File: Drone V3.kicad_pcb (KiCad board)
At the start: 4 copper layers, 96 parts, among them J2 Phase Outputs, J3 Pad Terminals, J4 Signal, U1 IRS21867S, U13 STM32F303CBTx, U4 INA180A3, U6 IRS21867S, U7 IRS21867S, U8 INA180A3, U9 INA180A3

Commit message: Drone PCB Update
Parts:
- removed 12V_SD2: XL1509-12, Package_SO:SOIC-8_3.9x4.9mm_P1.27mm
- removed 3.3V_SD1: AP63203WU, Package_TO_SOT_SMD:TSOT-23-6
- removed 5V_SD1: XL1509-5, easyeda2kicad:SOIC-8_L5.0-W4.0-P1.27-LS6.0-BL
- removed D1, D6: SS34, easyeda2kicad:SMA_L4.3-W2.6-LS5.2-RD
- 12V_SD1: renamed from 12V; moved to B.Cu
- B: renamed from BOOT0_SW1; moved to B.Cu
- C15, C16, C17, C18, C19, C20, C21, C22, C23, C24, C25, C26, C27, C28, C39, C41, C42, C43, C45, C49, C50, C51, D10, D12, D8, L6, R10, R11, R12, R13, R14, R15, R16, R17, R18, R19, R20, R21, R22, R23, R24, R25, R26, R27, R28, R29, R30, R31, R34, R36, R37, R38, R39, R40, R9, ST-Link1, U1, U4, U6, U7, U8, U9: moved to B.Cu
- D14: value LED -> DBG1
- D15: value LED -> DBG2
- D17: value BuckLED -> BUCK
- R: renamed from NRST_SW1; moved to B.Cu
- U13: value STM32F303CBTx -> STM32
- moved NMOS2 154.6 mm to (48.3, 145.2), turned to 90 degrees
- moved NMOS3 149.7 mm to (36.9, 137.5), turned to 90 degrees
- moved NMOS4 125.6 mm to (48.3, 137.5), turned to 90 degrees
- moved NMOS1 124.2 mm to (36.9, 145.2), turned to 90 degrees
- moved C16 111.4 mm to (39.0, 145.5)
- moved NMOS5 111.4 mm to (36.9, 129.6), turned to 90 degrees
- moved R9 111.1 mm to (43.5, 145.5)
- moved C24 108.5 mm to (31.4, 140.5)
- moved R30 107.1 mm to (69.5, 150.5), turned to 90 degrees
- moved R10 105.7 mm to (43.5, 143.0)
- moved C18 104.6 mm to (52.5, 142.5), turned to 180 degrees
- moved C19 104.1 mm to (52.5, 145.0), turned to 180 degrees
- moved R31 103.6 mm to (67.0, 150.5), turned to -90 degrees
- moved B 102.6 mm to (73.5, 150.5), turned to 180 degrees
- moved R36 101.6 mm to (56.5, 145.0)
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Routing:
- net /ESC1/-ESC: track 14.6 -> 0.00 mm
- net /ESC1/+ESC: track 11.8 -> 0.00 mm
- net Net-(D15-A): track 2.62 -> 0.00 mm
- net Net-(D14-A): track 2.62 -> 0.00 mm
- net Net-(D17-K): track 2.56 -> 0.00 mm
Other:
- board outline added: 55 x 30 mm
- board text added: "12V"
- board text added: "DB1"
- board text added: "DB2"

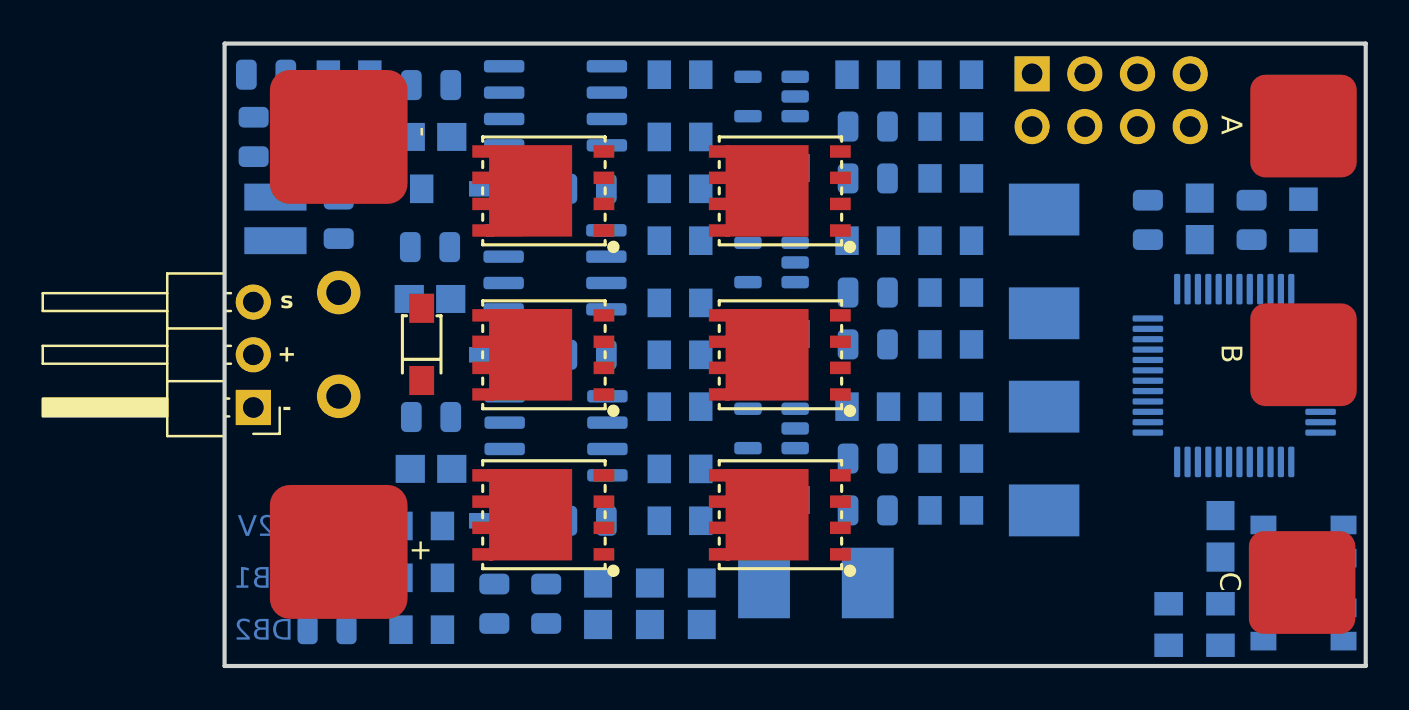
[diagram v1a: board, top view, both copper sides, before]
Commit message: ESC Routing, MOS Footprint Change
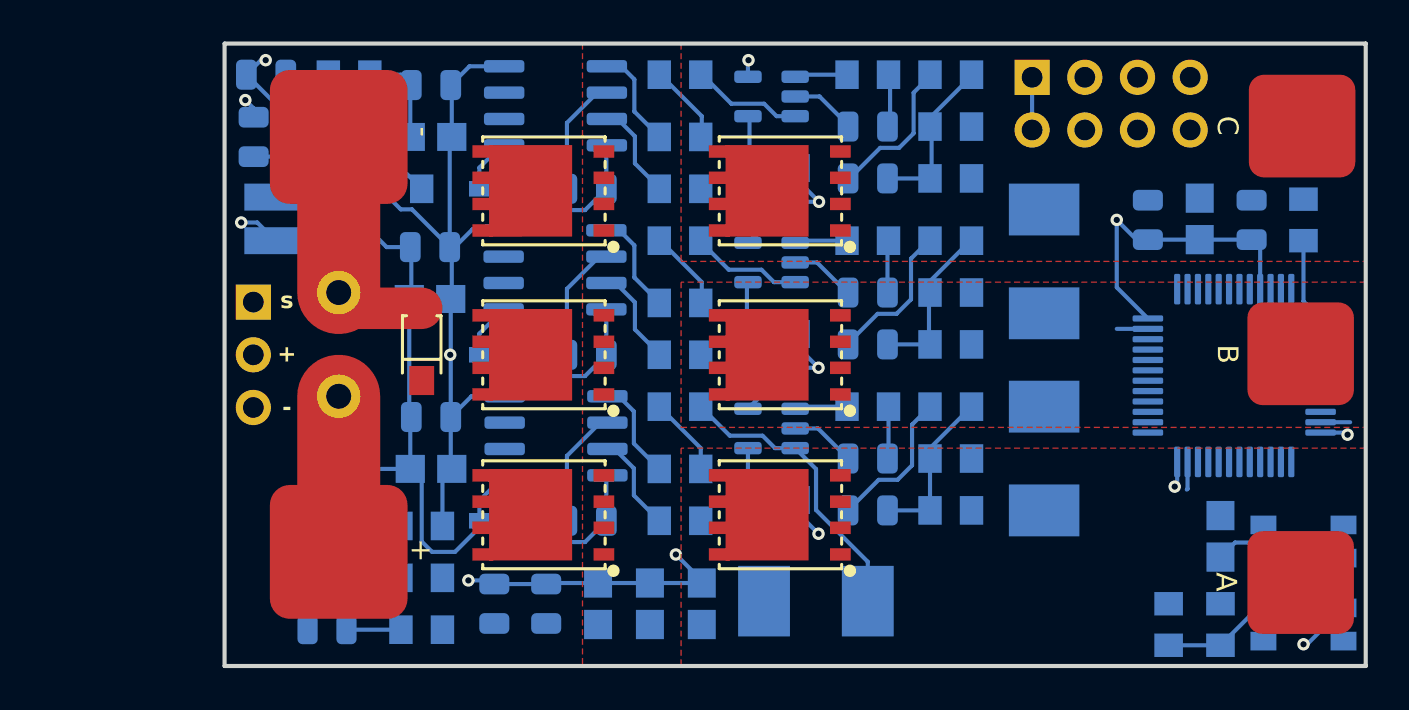
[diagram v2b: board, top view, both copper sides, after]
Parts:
- D14: value DBG1 -> LED
- D15: value DBG2 -> LED
- D17: value BUCK -> BuckLED
- J4: moved to B.Cu
- U13: value STM32 -> STM32F3
- moved J4 5.08 mm to (22.9, 135.0)
- moved R30 2.50 mm to (67.0, 150.5)
- moved R31 2.50 mm to (69.5, 150.5)
- moved R14 0.88 mm to (50.0, 149.4)
- moved ST-Link1 0.17 mm to (60.4, 124.1)
- turned C16 to 180 degrees
- turned C19 to 0 degrees
- turned C22 to 180 degrees
- turned C25 to 0 degrees
- turned C41 to 180 degrees
- turned C45 to -90 degrees
- turned C49 to 0 degrees
- turned J2 to 90 degrees
- renumbered B to B0, R to RST
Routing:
- net /ESC1/+3V3MCU: track 0.00 -> 162.6 mm, vias 0 -> 10
- net /ESC1/-ESC: track 0.00 -> 84.5 mm, vias 0 -> 2
- net /ESC1/+12V: track 0.00 -> 44.5 mm
- net /ESC1/BUCK_SW: track 0.00 -> 14.7 mm, vias 0 -> 2
- net Net-(NMOS2-S): track 0.00 -> 14.2 mm
- net /ESC1/BUCK_FB: track 0.00 -> 9.73 mm
- net Net-(C49-Pad2): track 0.00 -> 7.88 mm
- net Net-(C25-Pad2): track 0.00 -> 7.88 mm
- net Net-(C19-Pad2): track 0.00 -> 7.88 mm
- net /ESC1/+ESC: track 0.00 -> 7.50 mm
- net Net-(D8-K): track 0.00 -> 6.84 mm
- net Net-(D10-K): track 0.00 -> 6.82 mm
- net Net-(D12-K): track 0.00 -> 6.69 mm
- net /ESC1/NRST: track 0.00 -> 6.57 mm
- net /ESC1/A_Phase: track 0.00 -> 5.74 mm
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- added copper zone on F.Cu, net /ESC1/+ESC
- added copper zone on B.Cu, net /ESC1/-3V3MCU
- added copper zone on In2.Cu, net /ESC1/-3V3MCU
- added copper zone on In1.Cu, net /ESC1/-ESC
- added copper zone on F.Cu, net /ESC1/A_Phase
- added copper zone on F.Cu, net /ESC1/B_Phase
- added copper zone on F.Cu, net /ESC1/C_Phase

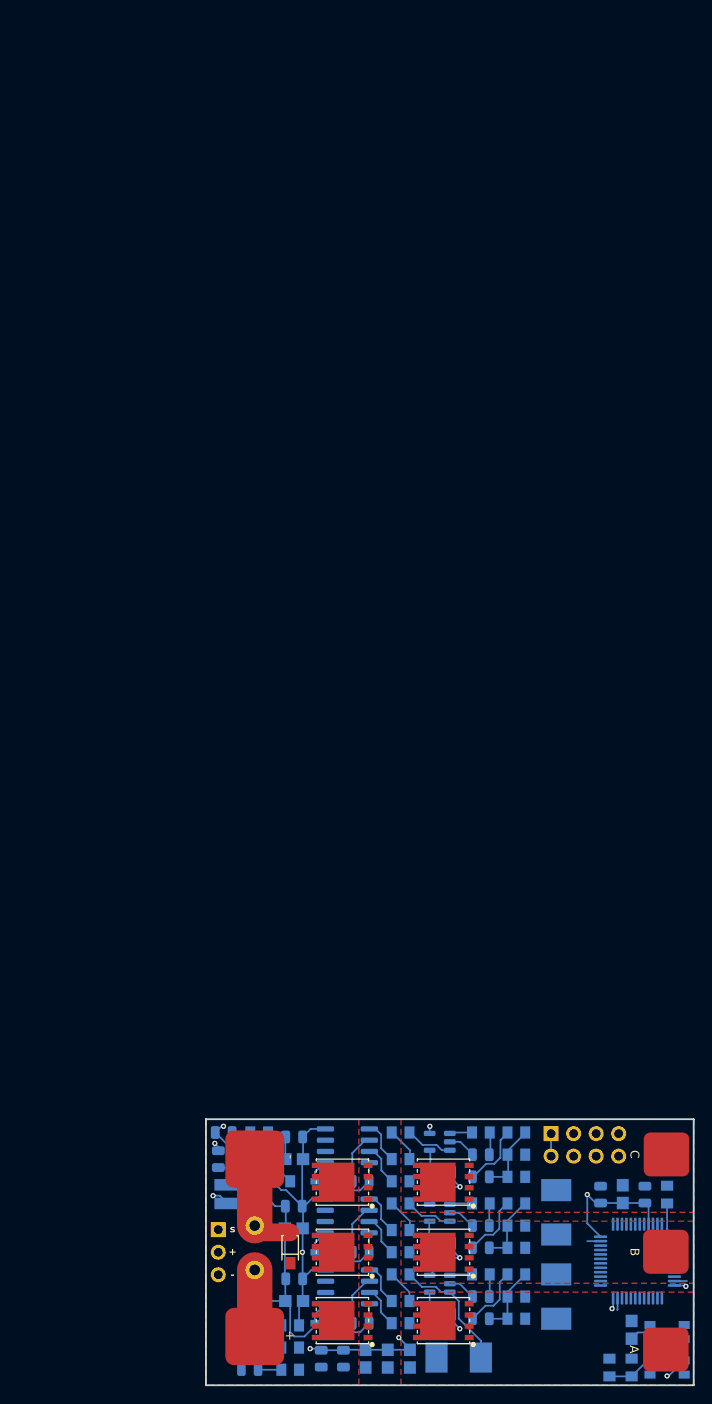
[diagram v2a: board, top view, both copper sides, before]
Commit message: Routing Update. Signal powers routed except for MCU. Look for unrouted traces without vias. Vias for signal lines added for organization
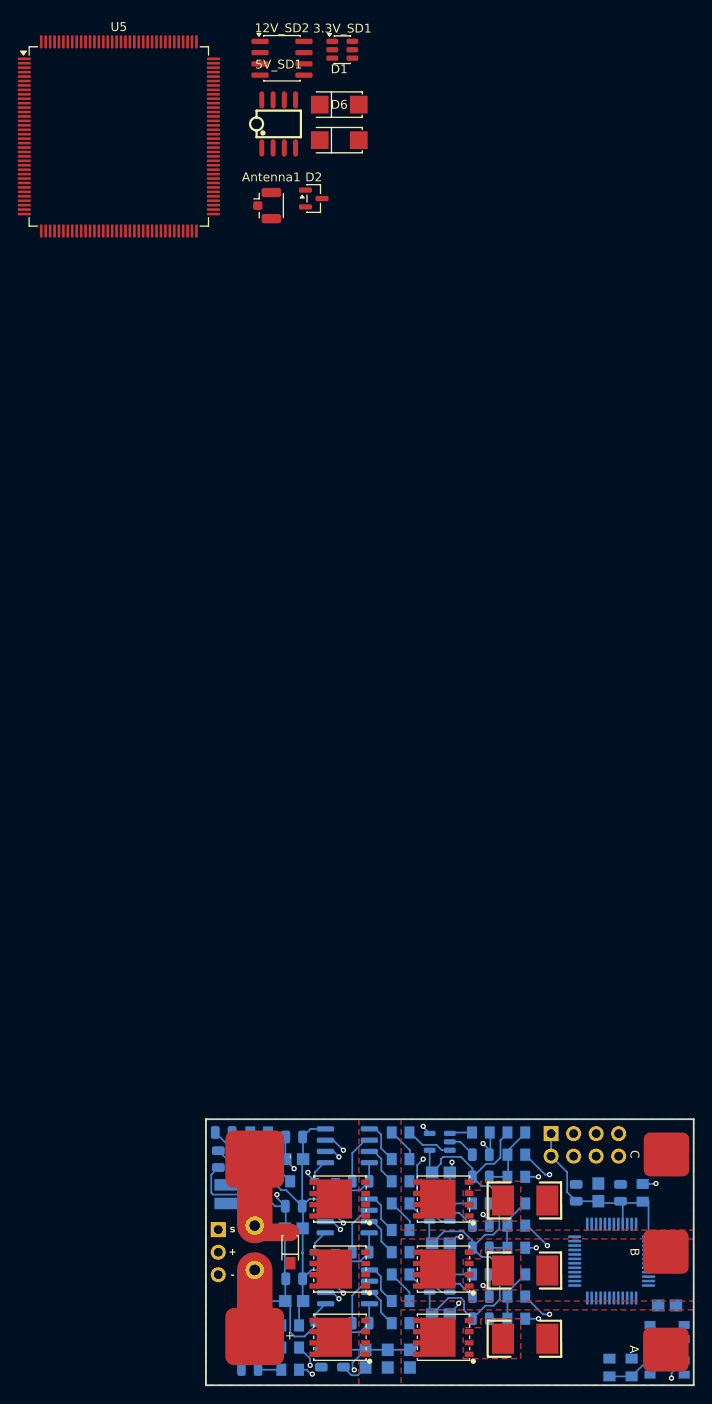
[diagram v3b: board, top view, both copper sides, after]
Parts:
- added 12V_SD2: XL1509-12, Package_SO:SOIC-8_3.9x4.9mm_P1.27mm, F.Cu at (30.1, 2.86)
- added 3.3V_SD1: AP63203WU, Package_TO_SOT_SMD:TSOT-23-6, F.Cu at (36.9, 1.90)
- added 5V_SD1: XL1509-5, easyeda2kicad:SOIC-8_L5.0-W4.0-P1.27-LS6.0-BL, F.Cu at (29.7, 10.3)
- added Antenna1: Conn_Coaxial, Connector_Coaxial:U.FL_Hirose_U.FL-R-SMT-1_Vertical, F.Cu at (28.4, 19.5)
- added D1: SS34, easyeda2kicad:SMA_L4.3-W2.6-LS5.2-RD, F.Cu at (36.5, 8.09)
- added D2: BAT54S, Package_TO_SOT_SMD:SOT-23, F.Cu at (33.7, 18.7)
- added D6: SS34, easyeda2kicad:SMA_L4.3-W2.6-LS5.2-RD, F.Cu at (36.5, 12.1)
- added U5: STM32F427ZGTx, Package_QFP:LQFP-144_20x20mm_P0.5mm, F.Cu at (11.7, 11.7)
- R14, R19, R26: moved to F.Cu
- U13: value STM32F3 -> STM32F303CBTx
- moved R14 7.79 mm to (57.5, 147.3), turned to 0 degrees
- moved C39 4.85 mm to (73.5, 143.5), turned to 180 degrees
- moved R19 4.57 mm to (57.5, 139.6), turned to 0 degrees
- moved R26 3.75 mm to (57.5, 131.7), turned to 0 degrees
- moved U13 2.91 mm to (67.2, 138.5)
- moved C36 2.76 mm to (68.2, 130.8)
- moved C37 2.76 mm to (65.8, 130.8)
- moved C38 2.76 mm to (63.2, 130.8)
- moved R34 2.76 mm to (70.8, 130.8)
- moved NMOS3 1.92 mm to (36.6, 139.4)
- moved NMOS5 1.92 mm to (36.6, 131.5)
- moved NMOS1 1.90 mm to (36.6, 147.1)
- moved NMOS4 1.90 mm to (48.3, 139.4)
- moved NMOS6 1.90 mm to (48.3, 131.5)
- moved NMOS2 1.88 mm to (48.3, 147.1)
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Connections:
- net Net-(NMOS2-S) renamed /ESC1/A_Shunt
- net Net-(NMOS4-S) renamed /ESC1/B_Shunt
- net Net-(NMOS6-S) renamed /ESC1/C_Shunt
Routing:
- net /ESC1/+3V3MCU: track 162.6 -> 109.3 mm, vias 10 -> 7
- net /ESC1/-ESC: track 84.5 -> 124.7 mm, vias 2 -> 0
- net /ESC1/+12V: track 44.5 -> 55.4 mm, vias 0 -> 3
- net /ESC1/A_Shunt: track 14.2 -> 5.38 mm
- net /ESC1/NRST: track 6.57 -> 0.00 mm
- net /ESC1/BUCK_SW: track 14.7 -> 8.34 mm, vias 2 -> 0
- net /ESC1/C_Phase: track 5.72 -> 9.40 mm, vias 0 -> 1
- net /ESC1/A_Phase: track 5.74 -> 9.32 mm, vias 0 -> 1
- net /ESC1/B_Phase: track 5.72 -> 9.15 mm, vias 0 -> 1
- net /ESC1/MCU_BL: track 0.00 -> 2.64 mm, vias 0 -> 1
- net /ESC1/MCU_AL: track 0.00 -> 2.55 mm, vias 0 -> 1
- net Net-(U13-PA0): track 0.00 -> 2.52 mm, vias 0 -> 1
- net /ESC1/MCU_CL: track 0.00 -> 2.50 mm, vias 0 -> 1
- net /ESC1/MCU_BH: track 0.00 -> 2.09 mm, vias 0 -> 1
- net /ESC1/MCU_AH: track 0.00 -> 1.79 mm, vias 0 -> 1
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- added copper zone on F.Cu, net /ESC1/A_Shunt
- added copper zone on F.Cu, net /ESC1/B_Shunt
- added copper zone on F.Cu, net /ESC1/C_Shunt

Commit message: Update Type stuff
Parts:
- removed 12V_SD2: XL1509-12, Package_SO:SOIC-8_3.9x4.9mm_P1.27mm
- removed 3.3V_SD1: AP63203WU, Package_TO_SOT_SMD:TSOT-23-6
- removed 5V_SD1: XL1509-5, easyeda2kicad:SOIC-8_L5.0-W4.0-P1.27-LS6.0-BL
- removed Antenna1: Conn_Coaxial, Connector_Coaxial:U.FL_Hirose_U.FL-R-SMT-1_Vertical
- removed C17, C50: 100n, easyeda2kicad:C0805
- removed C18, C51: 22n, Capacitor_SMD:C_0805_2012Metric
- removed D1, D6: SS34, easyeda2kicad:SMA_L4.3-W2.6-LS5.2-RD
- removed D2: BAT54S, Package_TO_SOT_SMD:SOT-23
- removed R14: 6E-4, easyeda2kicad:RES-SMD_L6.4-W3.2_LRS2512
- removed R15: 220, easyeda2kicad:R0805
- removed U5: STM32F427ZGTx, Package_QFP:LQFP-144_20x20mm_P0.5mm
- removed U8: INA180A3, Package_TO_SOT_SMD:SOT-23-5
- added C29: 100n, easyeda2kicad:C0805, B.Cu at (50.8, 148.0)
- added C40: 22n, Capacitor_SMD:C_0805_2012Metric, B.Cu at (56.0, 144.9)
- moved D17 48.7 mm to (74.9, 140.2), turned to 90 degrees
- moved D14 46.9 mm to (72.6, 140.2), turned to -90 degrees
- moved D15 45.1 mm to (70.3, 140.2), turned to -90 degrees
- moved R35 43.9 mm to (74.9, 144.2), turned to -90 degrees
- moved R32 41.8 mm to (72.6, 144.2), turned to 90 degrees
- moved R33 39.8 mm to (70.3, 144.2), turned to 90 degrees
- moved 12V_SD1 23.4 mm to (26.2, 150.5)
- moved C42 23.4 mm to (23.0, 150.3)
- moved R39 23.3 mm to (26.2, 147.3)
- moved C43 22.6 mm to (23.0, 146.6), turned to 90 degrees
- moved C23 21.9 mm to (30.6, 146.3)
- moved C28 21.7 mm to (30.4, 148.7)
- moved R40 21.5 mm to (30.3, 151.0), turned to 0 degrees
- moved R29 21.0 mm to (53.9, 144.9), turned to -90 degrees
- moved U9 20.1 mm to (50.5, 144.9)
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- renumbered B0 to BOOT0_SW1, RST to NRST_SW1
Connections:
- C27 pad 1: /ESC1/MCU_BI -> /ESC1/MCU_CI
- NMOS2 pad 3: /ESC1/A_Shunt -> /ESC1/Shunt_A
- NMOS4 pad 3: /ESC1/B_Shunt -> /ESC1/-ESC
- NMOS6 pad 3: /ESC1/C_Shunt -> /ESC1/Shunt_C
- R11 pad 2: /ESC1/A_Shunt -> /ESC1/Shunt_A
- R18 pad 2: /ESC1/B_Shunt -> /ESC1/-ESC
- R19 pad 1: /ESC1/B_Shunt -> /ESC1/Shunt_C
- R22 pad 2: /ESC1/MCU_BI -> /ESC1/MCU_CI
- R25 pad 2: /ESC1/C_Shunt -> /ESC1/Shunt_C
- R26 pad 1: /ESC1/C_Shunt -> /ESC1/Shunt_A
- R29 pad 2: /ESC1/MCU_CI -> /ESC1/MCU_AI
- U13 pad 26: /ESC1/MCU_BI -> unconnected-(U13-PB13-Pad26)
- U4 pad 3: /ESC1/B_Shunt -> /ESC1/Shunt_C
- U9 pad 3: /ESC1/C_Shunt -> /ESC1/Shunt_A
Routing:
- net /ESC1/-ESC: track 124.7 -> 10.2 mm, vias 0 -> 176
- net /ESC1/+3V3MCU: track 109.3 -> 26.3 mm, vias 7 -> 2
- net /ESC1/+12V: track 55.4 -> 13.7 mm, vias 3 -> 0
- net /ESC1/Shunt_C: track 0.00 -> 31.4 mm, vias 0 -> 3
- net Net-(NMOS6-G): track 3.83 -> 22.7 mm, vias 0 -> 2
- net /ESC1/C_Phase: track 9.40 -> 23.7 mm, vias 1 -> 2
- net Net-(NMOS5-G): track 0.00 -> 13.3 mm, vias 0 -> 3
- net /ESC1/BUCK_FB: track 9.73 -> 0.00 mm
- net /ESC1/BUCK_SW: track 8.34 -> 0.00 mm
- net Net-(C19-Pad2): track 7.88 -> 0.00 mm
- net Net-(R22-Pad1): track 2.40 -> 8.90 mm
- net /ESC1/C_Shunt: track 5.38 -> 0.00 mm
- net /ESC1/B_Shunt: track 5.38 -> 0.00 mm
- net /ESC1/A_Shunt: track 5.38 -> 0.00 mm
- net Net-(NMOS2-G): track 3.83 -> 9.18 mm, vias 0 -> 1
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- added copper zone on In2.Cu, net /ESC1/+ESC
- added copper zone on F.Cu, net /ESC1/-ESC
- added copper zone on F.Cu, net /ESC1/Shunt_A
- added copper zone on F.Cu, net /ESC1/Shunt_C
- removed copper zone on B.Cu, net /ESC1/-3V3MCU
- removed copper zone on In2.Cu, net /ESC1/-3V3MCU
- removed copper zone on F.Cu, net /ESC1/A_Shunt
- removed copper zone on F.Cu, net /ESC1/B_Shunt
- removed copper zone on F.Cu, net /ESC1/C_Shunt
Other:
- board size 55 x 30 mm -> 55 x 42 mm
